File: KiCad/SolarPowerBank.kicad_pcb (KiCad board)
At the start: 2 copper layers, 48.3 x 27.9 mm, 31 parts, among them J1 Solar, J2 JST PH2, J3 Conn_01x04, J4 USB_A, U1 SW2303, U2 BQ25185

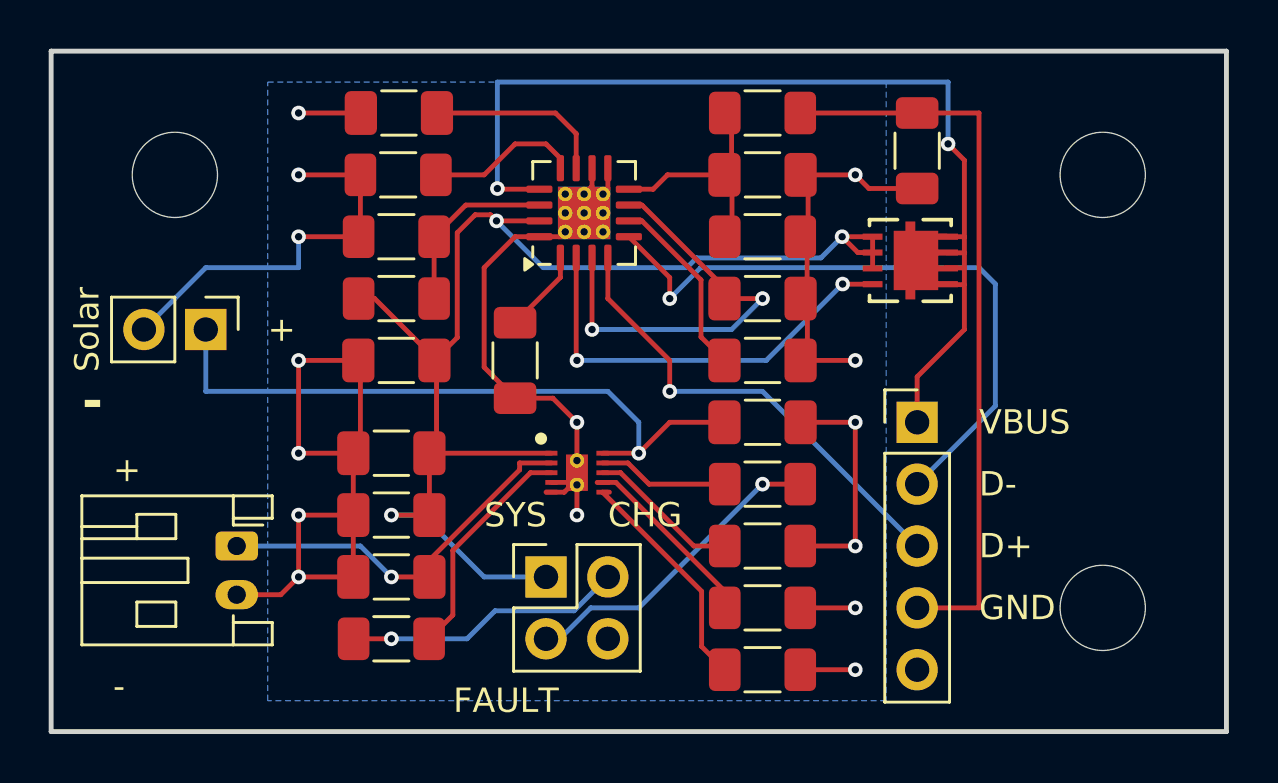
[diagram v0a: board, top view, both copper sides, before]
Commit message: Changed footprints to allow for easier hand soldering
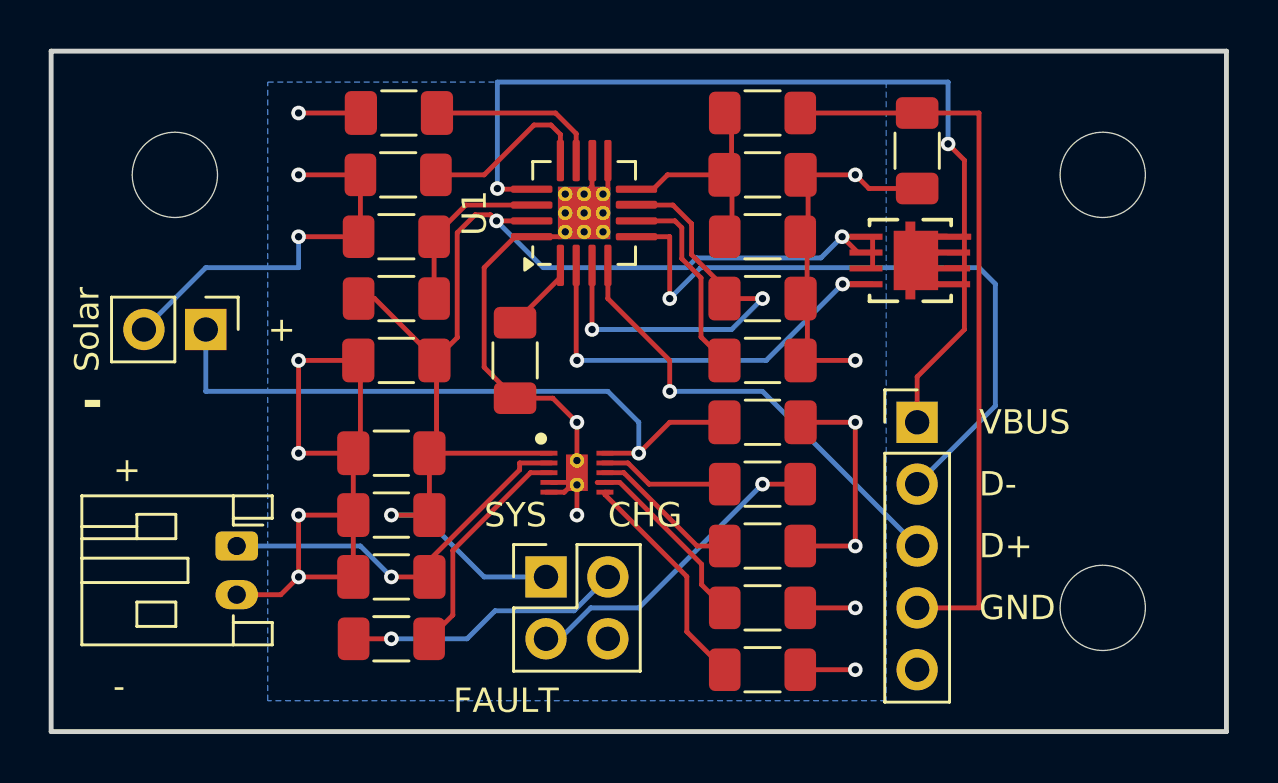
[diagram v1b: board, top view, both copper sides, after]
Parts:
- MOSFET1: footprint SolarPowerBankLibrary:DFN3x3A_8L_EP1_P -> SolarPowerBankLibrary:DFN3x3A_8L_EP1_P_HandSoldering
- U1: footprint Package_DFN_QFN:QFN-16-1EP_4x4mm_P0.65mm_EP2.15x2.15mm_ThermalVias -> SolarPowerBankLibrary:QFN-16-1EP_4x4mm_P0.65mm_EP2.15x2.15mm_ThermalVias-HandSolder
- U2: footprint SolarPowerBankLibrary:WSON-10-1EP_2.2x2.0mm_P0.4_ThermalVias -> SolarPowerBankLibrary:WSON-10-1EP_2.2x2.0mm_P0.4_ThermalVias-HandSolder
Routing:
- net /DM: track 27.0 -> 23.7 mm
- net Net-(U1-PSET): track 6.29 -> 7.51 mm
- net Net-(U1-CC1): track 7.67 -> 8.46 mm
- net /VDD: track 18.0 -> 18.7 mm
